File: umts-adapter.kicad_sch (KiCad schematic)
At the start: 10 parts, among them J1 Conn_02x15_Counter_Clockwise, J2 DB9_Female_MountingHoles, J3 Conn_02x01, U1 L7805

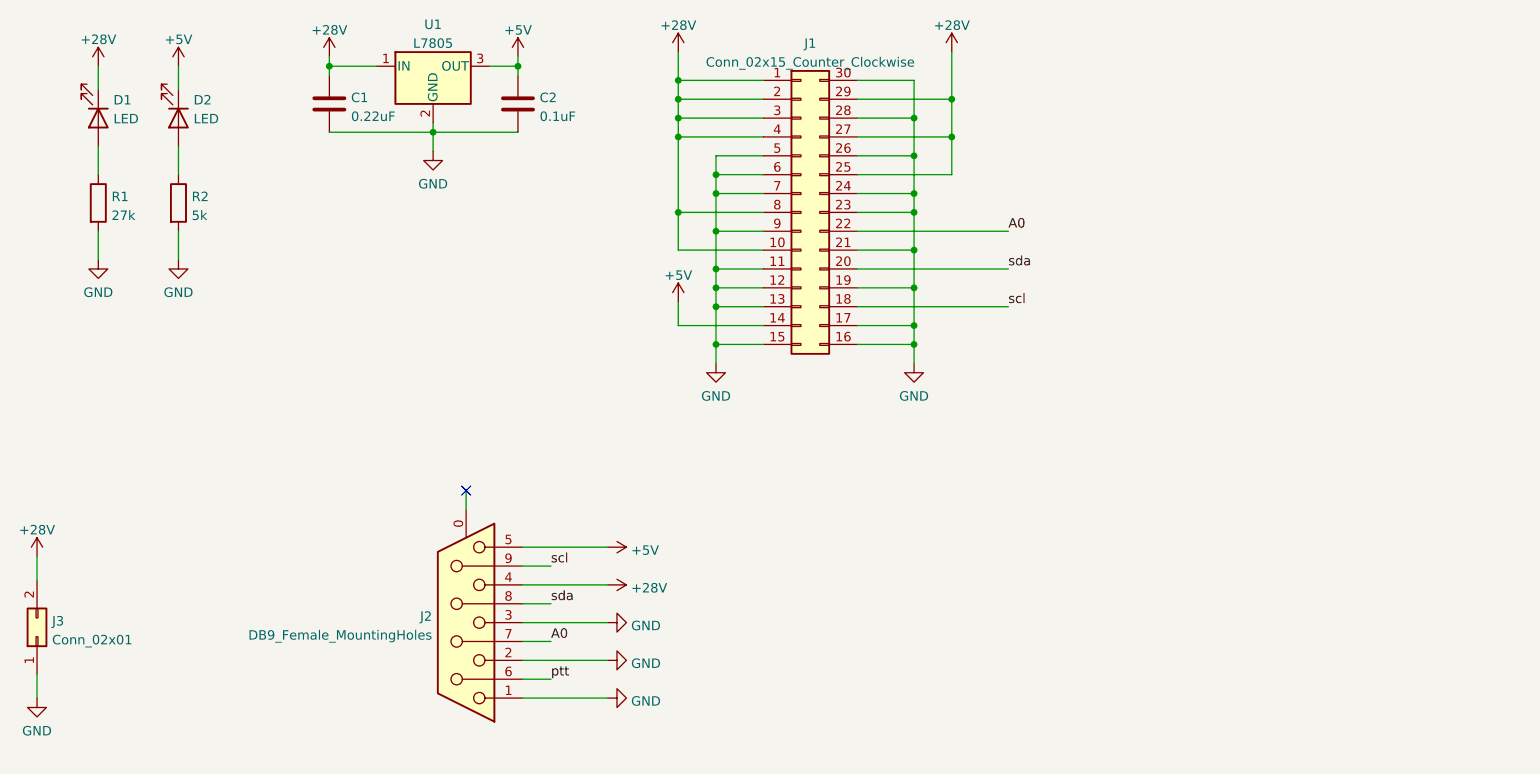
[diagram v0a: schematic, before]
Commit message: feat: rev1.0, fits without cover. To be redesigned
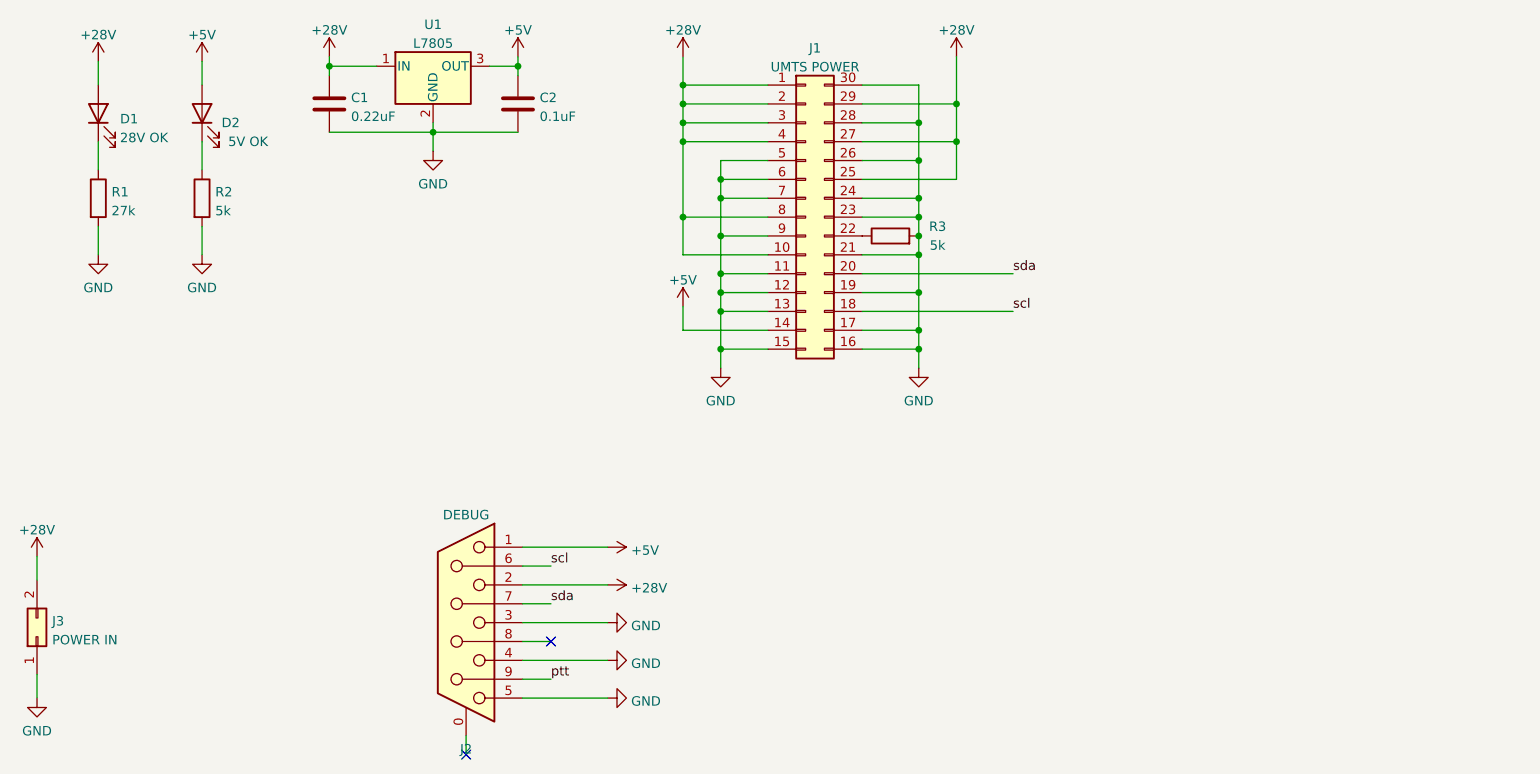
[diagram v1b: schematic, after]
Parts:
- added R3: 5k, Resistor_SMD:R_0805_2012Metric_Pad1.20x1.40mm_HandSolder, symbol Device:R
- C1, C2: footprint Capacitor_SMD:C_0805_2012Metric_Pad1.18x1.45mm_HandSolder -> Capacitor_SMD:C_0603_1608Metric_Pad1.08x0.95mm_HandSolder
- D1: value LED -> 28V OK
- D2: value LED -> 5V OK
- J1: value Conn_02x15_Counter_Clockwise -> UMTS POWER
- J2: value DB9_Female_MountingHoles -> DEBUG
- J3: value Conn_02x01 -> POWER IN
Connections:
- net +28V: now also D1.2 (A), J2.2; no longer D1.1 (K), J2.4
- net +5V: now also D2.2 (A), J2.1; no longer D2.1 (K), J2.5
- net GND: now also J2.4, J2.5, R3.2; no longer J2.1, J2.2
- net ptt: now also J2.9; no longer J2.6
- net scl: now also J2.6; no longer J2.9
- net sda: now also J2.7; no longer J2.8
- net at R2.1: now also D2.1 (K); no longer D2.2 (A)
- net at R1.1: now also D1.1 (K); no longer D1.2 (A)
- net A0: no longer names the net of J1.22 (Pin_22)
- net A0: now also R3.1; no longer J2.7
- no-connect marks 1 -> 2
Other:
- moved on the sheet: D1, D2, J1, J2, R1, R2

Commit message: !change: updated pcb to fit into built-in holes on the box change: two-stage adjustable regulators
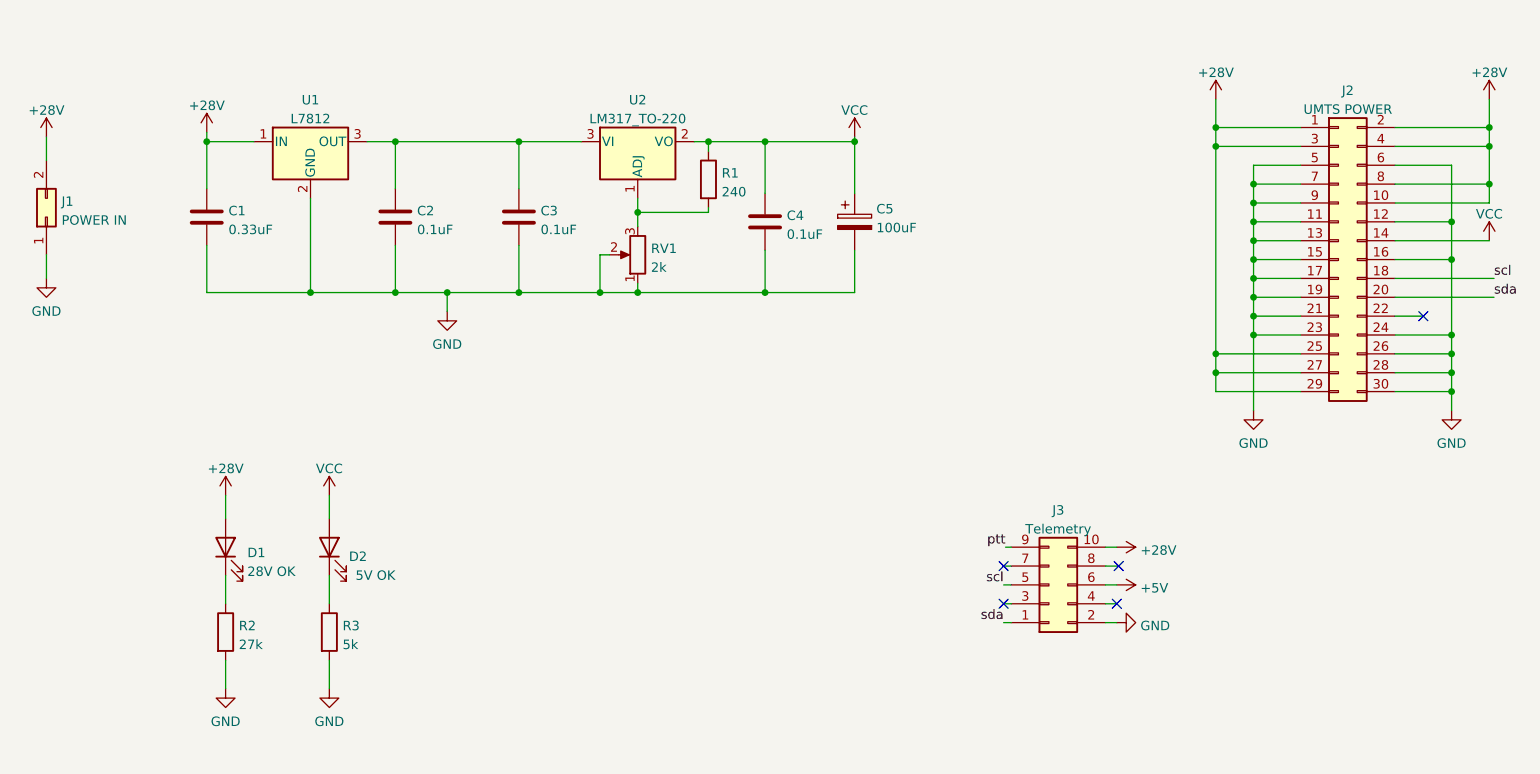
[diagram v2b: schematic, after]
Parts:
- removed J2: DEBUG, Connector_Dsub:DSUB-9_Female_Horizontal_P2.77x2.84mm_EdgePinOffset4.94mm_Housed_MountingHolesOffset7.48mm, symbol Connector:DB9_Female_MountingHoles
- removed R3: 5k, Resistor_SMD:R_0805_2012Metric_Pad1.20x1.40mm_HandSolder, symbol Device:R
- added C3, C4: 0.1uF, Capacitor_SMD:C_0603_1608Metric_Pad1.08x0.95mm_HandSolder, symbol Device:C
- added C5: 100uF, Capacitor_THT:CP_Radial_D8.0mm_P3.50mm, symbol Device:C_Polarized
- added J3: Telemetry, Connector_PinHeader_2.54mm:PinHeader_2x05_P2.54mm_Vertical, symbol Connector_Generic:Conn_02x05_Odd_Even
- added R1: 240, Resistor_SMD:R_0805_2012Metric_Pad1.20x1.40mm_HandSolder, symbol Device:R
- added RV1: 2k, Potentiometer_THT:Potentiometer_Bourns_3266Y_Vertical, symbol Device:R_Potentiometer
- added U2: LM317_TO-220, Package_TO_SOT_THT:TO-220-3_Vertical, symbol Regulator_Linear:LM317_TO-220
- C1: value 0.22uF -> 0.33uF
- J2: renamed from J1; symbol Connector_Generic:Conn_02x15_Counter_Clockwise -> Connector_Generic:Conn_02x15_Odd_Even
- U1: value L7805 -> L7812; symbol Regulator_Linear:L7805 -> Regulator_Linear:L7812
- renumbered J3 to J1, R1 to R2, R2 to R3
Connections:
- net +28V: now also J3.10 (Pin_10)
- net +5V: now also J3.6 (Pin_6); no longer C2.1, D2.2 (A), J2.14 (Pin_14), U1.3 (OUT)
- net GND: now also C3.2, C4.2, C5.2, J3.2 (Pin_2), RV1.1, RV1.2
- net ptt: now also J3.9 (Pin_9)
- net scl: now also J3.5 (Pin_5)
- net sda: now also J3.1 (Pin_1)
- new net: C2.1, C3.1, U1.3 (OUT), U2.3 (VI)
- new net: R1.2, RV1.3, U2.1 (ADJ)
- new net VCC: C4.1, C5.1, D2.2 (A), J2.14 (Pin_14), R1.1, U2.2 (VO)
- no-connect marks 2 -> 5
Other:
- moved on the sheet: C1, C2, D1, D2, J1, J2, R2, R3, U1

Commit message: feat!: removed all extra components to make it just a breakout
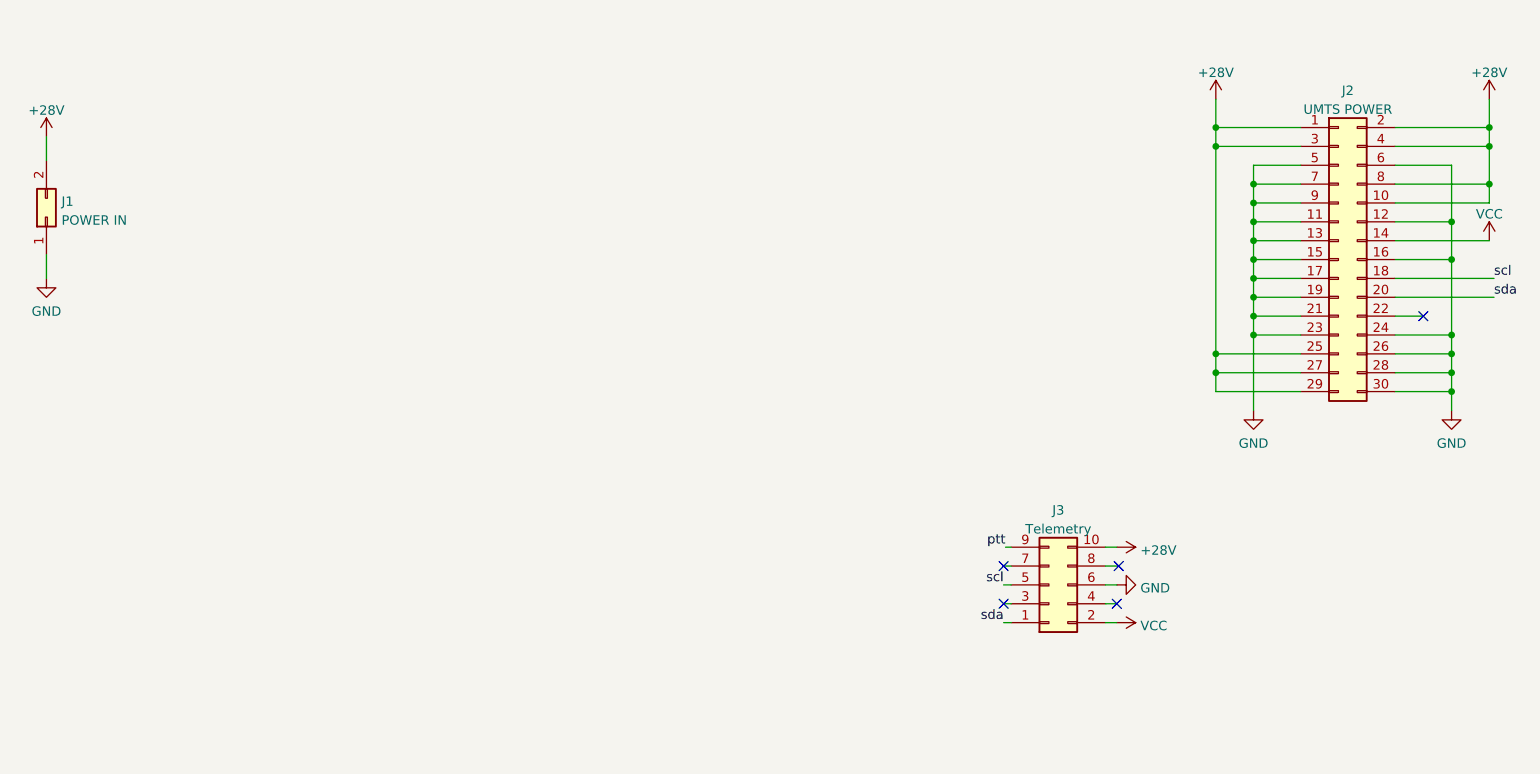
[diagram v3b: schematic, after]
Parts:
- removed C1: 0.33uF, Capacitor_SMD:C_0603_1608Metric_Pad1.08x0.95mm_HandSolder, symbol Device:C
- removed C2, C3, C4: 0.1uF, Capacitor_SMD:C_0603_1608Metric_Pad1.08x0.95mm_HandSolder, symbol Device:C
- removed C5: 100uF, Capacitor_THT:CP_Radial_D8.0mm_P3.50mm, symbol Device:C_Polarized
- removed D1: 28V OK, LED_THT:LED_D3.0mm, symbol Device:LED
- removed D2: 5V OK, LED_THT:LED_D3.0mm, symbol Device:LED
- removed R1: 240, Resistor_SMD:R_0805_2012Metric_Pad1.20x1.40mm_HandSolder, symbol Device:R
- removed R2: 27k, Resistor_SMD:R_0805_2012Metric_Pad1.20x1.40mm_HandSolder, symbol Device:R
- removed R3: 5k, Resistor_SMD:R_0805_2012Metric_Pad1.20x1.40mm_HandSolder, symbol Device:R
- removed RV1: 2k, Potentiometer_THT:Potentiometer_Bourns_3266Y_Vertical, symbol Device:R_Potentiometer
- removed U1: L7812, Package_TO_SOT_THT:TO-220-3_Vertical, symbol Regulator_Linear:L7812
- removed U2: LM317_TO-220, Package_TO_SOT_THT:TO-220-3_Vertical, symbol Regulator_Linear:LM317_TO-220
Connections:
- net +5V is gone; now on net GND: J3.6 (Pin_6)
- net GND: no longer J3.2 (Pin_2)
- net VCC: now also J3.2 (Pin_2)
